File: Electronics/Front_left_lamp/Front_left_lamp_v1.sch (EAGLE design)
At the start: 9 parts

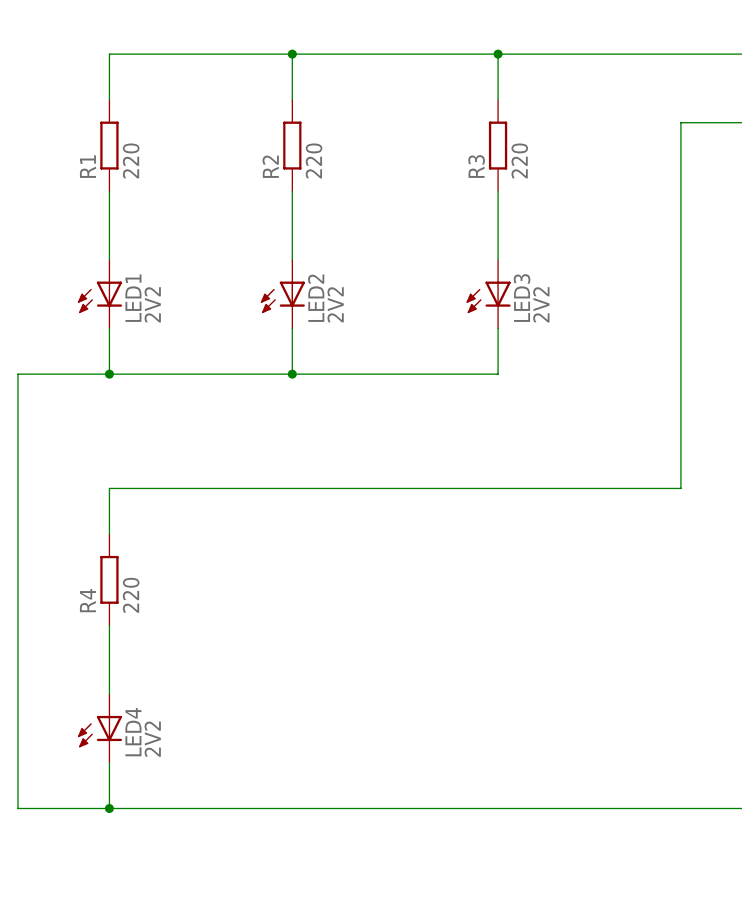
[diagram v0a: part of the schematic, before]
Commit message: List of parts updated
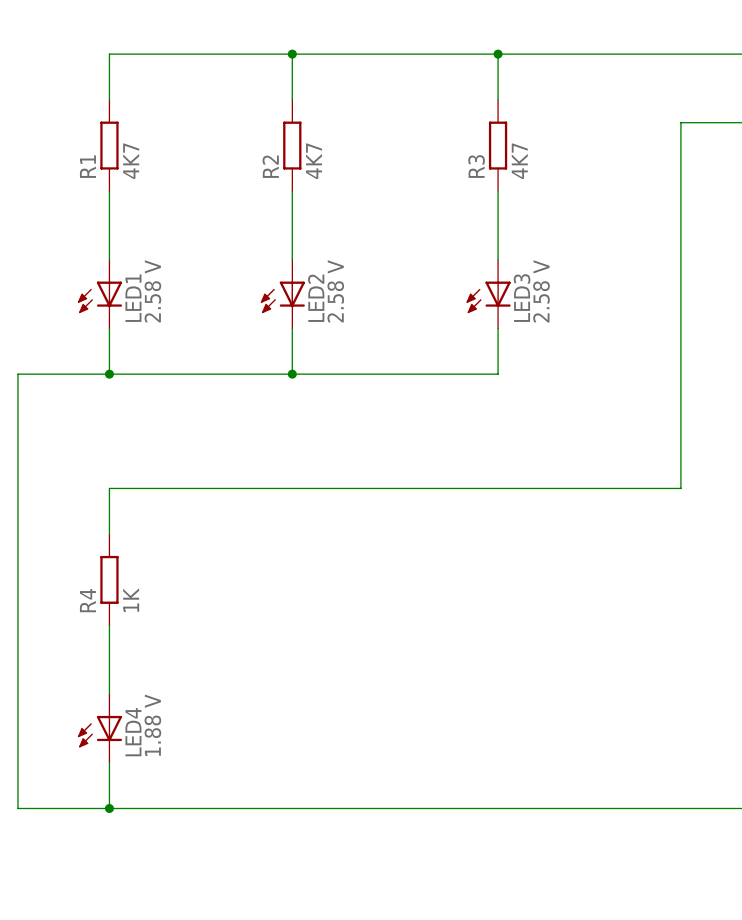
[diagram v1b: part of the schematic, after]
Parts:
- LED1, LED2, LED3: value 2V2 -> 2.58 V; CURRENT (none) -> 0.14 mA
- LED4: value 2V2 -> 1.88 V; CURRENT (none) -> 1.42 mA
- R1, R2, R3: value 220 -> 4K7
- R4: value 220 -> 1K
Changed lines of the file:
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@@
 <parts>
 <part name="FRAME1" library="frames" deviceset="FRAME_A_L" device="" value="Main"/>
-<part name="LED1" library="led" deviceset="LED" device="5MM" value="2V2"/>
-<part name="LED2" library="led" deviceset="LED" device="5MM" value="2V2"/>
-<part name="LED3" library="led" deviceset="LED" device="5MM" value="2V2"/>
-<part name="LED4" library="led" deviceset="LED" device="5MM" value="2V2"/>
-<part name="R1" library="resistor" deviceset="R-EU_" device="0204/2V" value="220"/>
-<part name="R2" library="resistor" deviceset="R-EU_" device="0204/2V" value="220"/>
-<part name="R3" library="resistor" deviceset="R-EU_" device="0204/2V" value="220"/>
-<part name="R4" library="resistor" deviceset="R-EU_" device="0204/2V" value="220"/>
+<part name="LED1" library="led" deviceset="LED" device="5MM" value="2.58 V">
+<attribute name="CURRENT" value="0.14 mA"/>
+</part>
+<part name="LED2" library="led" deviceset="LED" device="5MM" value="2.58 V">
+<attribute name="CURRENT" value="0.14 mA"/>
+</part>
+<part name="LED3" library="led" deviceset="LED" device="5MM" value="2.58 V">
+<attribute name="CURRENT" value="0.14 mA"/>
+</part>
+<part name="LED4" library="led" deviceset="LED" device="5MM" value="1.88 V">
+<attribute name="CURRENT" value="1.42 mA"/>
+</part>
+<part name="R1" library="resistor" deviceset="R-EU_" device="0204/2V" value="4K7"/>
+<part name="R2" library="resistor" deviceset="R-EU_" device="0204/2V" value="4K7"/>
+<part name="R3" library="resistor" deviceset="R-EU_" device="0204/2V" value="4K7"/>
+<part name="R4" library="resistor" deviceset="R-EU_" device="0204/2V" value="1K"/>
 <part name="JP1" library="pinhead" deviceset="PINHD-2X2" device="" value="2X2"/>
 </parts>
@@
 <instance part="FRAME1" gate="G$1" x="0" y="0"/>
 <instance part="FRAME1" gate="G$2" x="172.72" y="0"/>
-<instance part="LED1" gate="G$1" x="81.28" y="144.78"/>
-<instance part="LED2" gate="G$1" x="101.6" y="144.78"/>
-<instance part="LED3" gate="G$1" x="124.46" y="144.78"/>
-<instance part="LED4" gate="G$1" x="81.28" y="96.52"/>
+<instance part="LED1" gate="G$1" x="81.28" y="144.78">
+<attribute name="CURRENT" x="81.28" y="144.78" size="1.778" layer="96" display="off"/>
+</instance>
+<instance part="LED2" gate="G$1" x="101.6" y="144.78">
+<attribute name="CURRENT" x="101.6" y="144.78" size="1.778" layer="96" display="off"/>
+</instance>
+<instance part="LED3" gate="G$1" x="124.46" y="144.78">
+<attribute name="CURRENT" x="124.46" y="144.78" size="1.778" layer="96" display="off"/>
+</instance>
+<instance part="LED4" gate="G$1" x="81.28" y="96.52">
+<attribute name="CURRENT" x="81.28" y="96.52" size="1.778" layer="96" display="off"/>
+</instance>
 <instance part="R1" gate="G$1" x="81.28" y="160.02" rot="R90"/>
 <instance part="R2" gate="G$1" x="101.6" y="160.02" rot="R90"/>

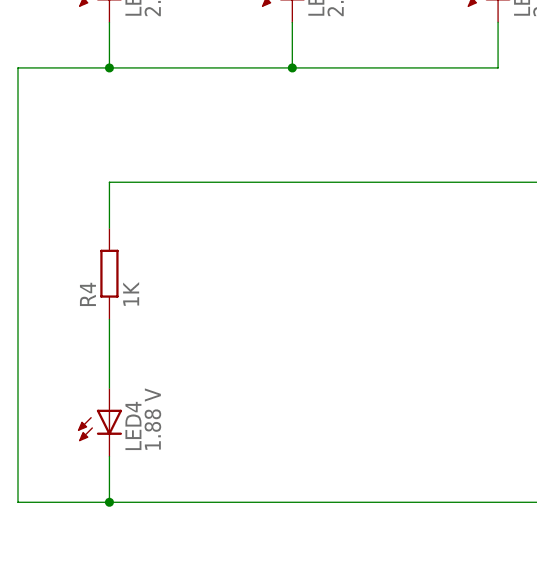
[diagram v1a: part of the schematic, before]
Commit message: Front lamps done
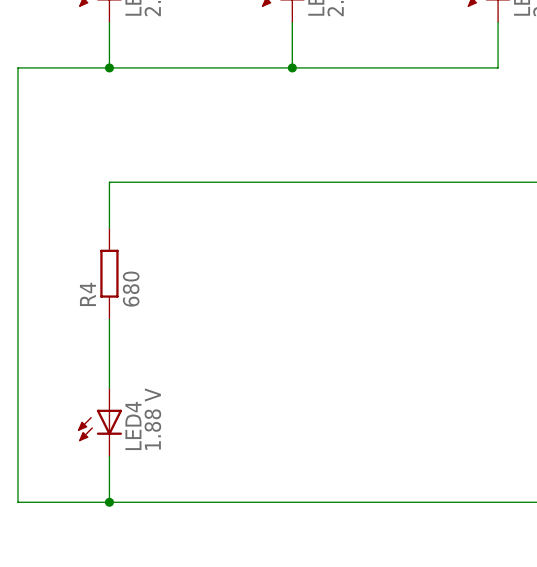
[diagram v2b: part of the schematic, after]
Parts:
- R4: value 1K -> 680
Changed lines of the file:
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@@
 <part name="R2" library="resistor" deviceset="R-EU_" device="0204/2V" value="4K7"/>
 <part name="R3" library="resistor" deviceset="R-EU_" device="0204/2V" value="4K7"/>
-<part name="R4" library="resistor" deviceset="R-EU_" device="0204/2V" value="1K"/>
+<part name="R4" library="resistor" deviceset="R-EU_" device="0204/2V" value="680"/>
 <part name="JP1" library="pinhead" deviceset="PINHD-2X2" device="" value="2X2"/>
 </parts>
